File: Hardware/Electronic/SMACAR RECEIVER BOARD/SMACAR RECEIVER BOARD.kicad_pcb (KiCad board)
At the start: 2 copper layers, 9 parts, among them J1 M04POLAR, J2 USB_C_Receptacle_USB2.0_14P, U1 ESP32-S3-DevKitC

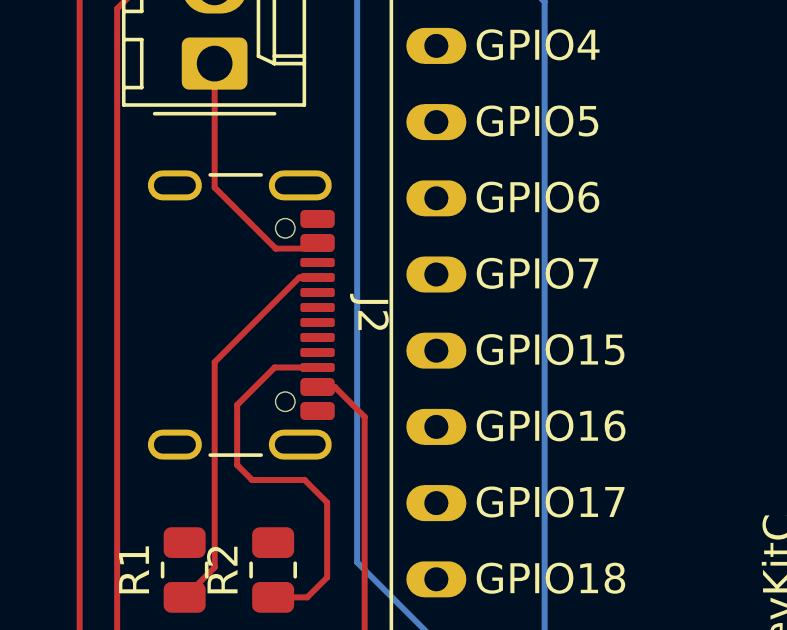
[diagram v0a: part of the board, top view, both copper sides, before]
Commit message: arreglos en las conexiones de usb c
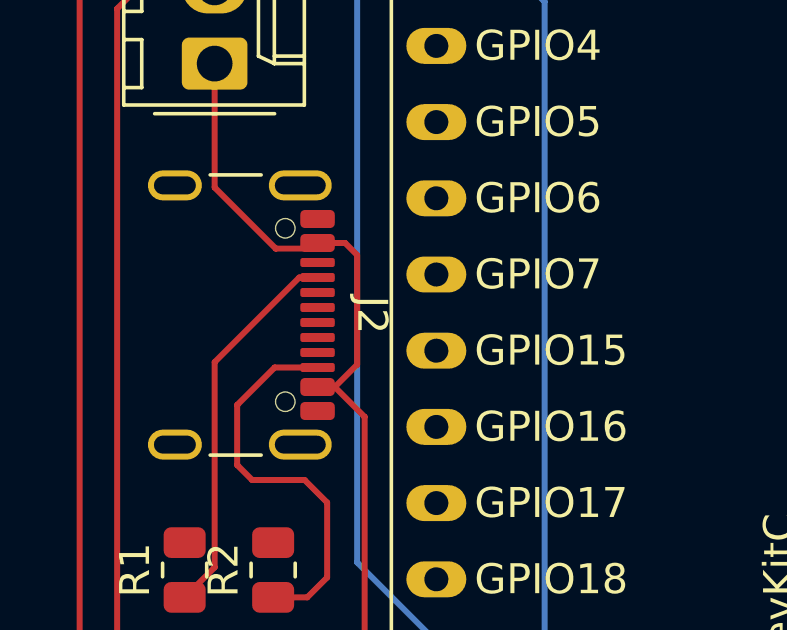
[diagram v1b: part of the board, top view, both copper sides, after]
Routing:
- net 5V: track 42.3 -> 48.5 mm
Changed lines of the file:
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@@
+	)
+	(segment
+		(start 132.35 66.1)
+		(end 131.43 66.1)
+		(width 0.2)
+		(layer "F.Cu")
+		(net 1)
 	)
 	(segment
 		(start 130.036 66.286)
 		(end 131.244 66.286)
+		(width 0.2)
+		(layer "F.Cu")
+		(net 1)
+	)
+	(segment
+		(start 132.75 66.5)
+		(end 132.35 66.1)
 		(width 0.2)
 		(layer "F.Cu")
@@
 	)
 	(segment
+		(start 132.004999 70.9)
+		(end 132.75 70.154999)
+		(width 0.2)
+		(layer "F.Cu")
+		(net 1)
+	)
+	(segment
 		(start 128 60.12)
 		(end 128 64.25)
 		(width 0.2)
 		(layer "F.Cu")
+		(net 1)
+	)
+	(segment
+		(start 132.75 70.154999)
+		(end 132.75 66.5)
+		(width 0.2)
+		(layer "F.Cu")

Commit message: TVS
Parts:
- added U2: TVS0500DRV, Package_SON:WSON-6-1EP_2x2mm_P0.65mm_EP1x1.6mm, F.Cu at (127.1, 89.3)
- added U3: TVS0500DRV, Package_SON:WSON-6-1EP_2x2mm_P0.65mm_EP1x1.6mm, F.Cu at (127.4, 102.8)
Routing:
- net Net-(R3-Pad2): track 108.6 -> 194.5 mm
- net 5V: track 48.5 -> 68.1 mm, vias 0 -> 1
- net GND: track 0.00 -> 1.30 mm

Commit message: V1.0 Revision
Revision for V1.0 of the project. Includes production files for JLCPCB. Some footprints and schematic symbols were changed.
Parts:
- removed R1, R2: 470R_0805_350mW, Resistor_SMD:R_0805_2012Metric
- removed U2, U3: TVS0500DRV, Package_SON:WSON-6-1EP_2x2mm_P0.65mm_EP1x1.6mm
- added D1: SMF33A, Diode_SMD:D_SMF, F.Cu at (131.5, 92.0)
- added D2: SMF33A, Diode_SMD:D_SMF, F.Cu at (135.0, 53.0)
- added R1_5.1k1: 470R_0805_350mW, Resistor_SMD:R_0805_2012Metric_Pad1.20x1.40mm_HandSolder, F.Cu at (129.0, 97.0)
- added R2_5.1k1: 470R_0805_350mW, Resistor_SMD:R_0805_2012Metric_Pad1.20x1.40mm_HandSolder, F.Cu at (132.0, 114.0)
- J2: value USB_C_Receptacle_USB2.0_14P -> 2137160001; footprint Connector_USB:USB_C_Receptacle_GCT_USB4105-xx-A_16P_TopMnt_Horizontal -> XUNPU TYPEC-306DDW-ARP16:MOLEX_2137160001
- moved J2 37.3 mm to (124.3, 105.6)
- moved J1 26.2 mm to (127.0, 86.3)
- moved R4 8.64 mm to (134.0, 87.0), turned to 180 degrees
- moved R3 5.00 mm to (134.0, 79.0), turned to 180 degrees
- moved U1 3.37 mm to (138.7, 51.2)
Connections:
- J2 pad A8: (no net) -> unconnected-(J2-SBU1-PadA8)
- J2 pad B8: (no net) -> unconnected-(J2-SBU2-PadB8)
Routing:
- net Net-(D2-A1): track 194.5 -> 43.4 mm, vias 1 -> 0
- net SDA: track 92.7 -> 15.6 mm
- net 5V: track 68.1 -> 41.3 mm, vias 1 -> 0
- net SCL: track 41.7 -> 17.8 mm, vias 1 -> 0
- net Net-(J2-CC2): track 13.3 -> 17.3 mm
- net GND: track 1.30 -> 0.00 mm
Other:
- board outline added: 41.5 x 70 mm

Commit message: update
PCB Y CODIGO PROTOTIPO
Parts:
- removed D1, D2: SMF33A, Diode_SMD:D_SMF
- removed R1_5.1k1, R2_5.1k1: 470R_0805_350mW, Resistor_SMD:R_0805_2012Metric_Pad1.20x1.40mm_HandSolder
- added REF**: MountingHole_2.2mm_M2_DIN965_Pad, MountingHole:MountingHole_2.2mm_M2_DIN965_Pad, F.Cu at (126.5, 52.5)
- J2: value 2137160001 -> Conn_01x02; footprint XUNPU TYPEC-306DDW-ARP16:MOLEX_2137160001 -> Connector_Molex:Molex_KK-254_AE-6410-02A_1x02_P2.54mm_Vertical
- moved J2 9.11 mm to (128.0, 97.3), turned to 90 degrees
- moved REF** 4.01 mm to (162.0, 117.0)
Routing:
- net 5V: track 41.3 -> 22.5 mm
- net Net-(J2-CC2): track 17.3 -> 0.00 mm
- net Net-(J2-CC1): track 13.1 -> 0.00 mm

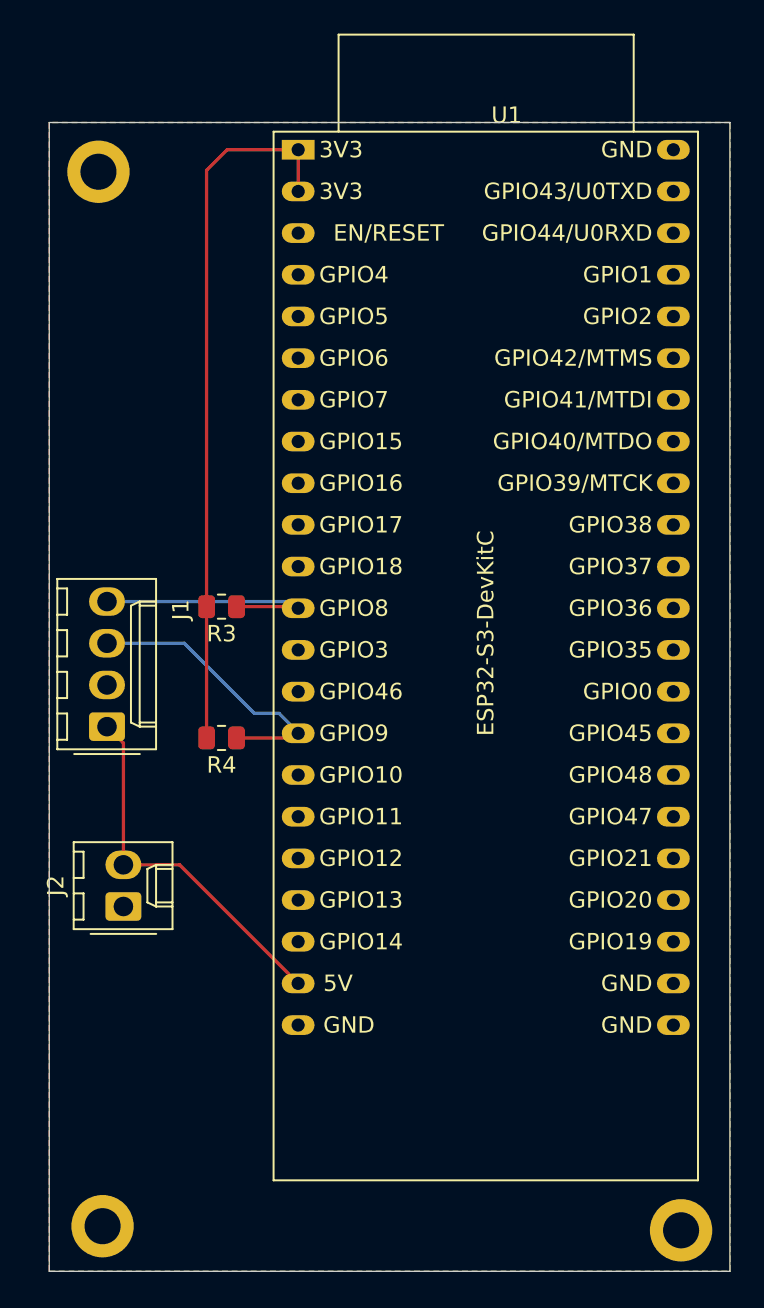
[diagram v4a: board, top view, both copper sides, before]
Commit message: PCB RECEPTOR MODIFICADA
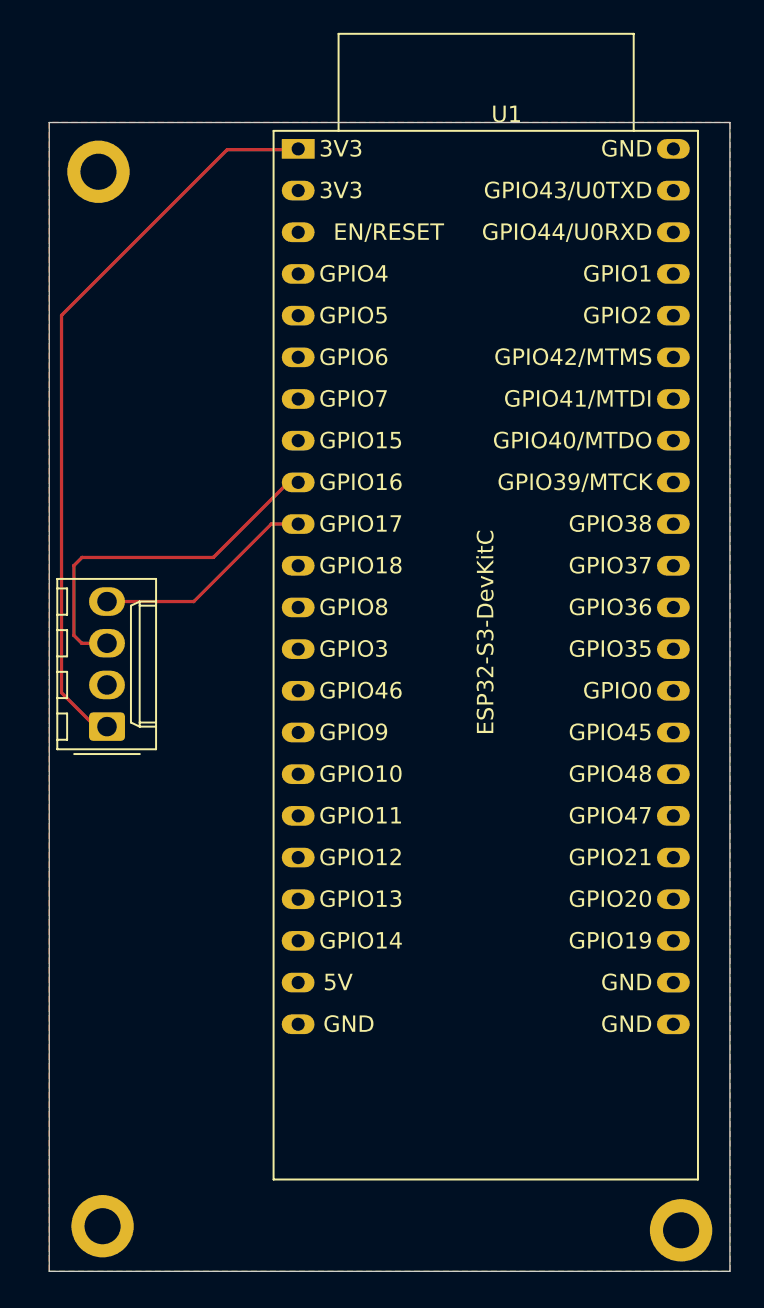
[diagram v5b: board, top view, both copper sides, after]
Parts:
- removed J2: Conn_01x02, Connector_Molex:Molex_KK-254_AE-6410-02A_1x02_P2.54mm_Vertical
- removed R3, R4: 470R_0805_350mW, Resistor_SMD:R_0805_2012Metric
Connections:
- J1 pad 1: 5V -> 3.3V
- J1 pad 3: SCL -> RX
- J1 pad 4: SDA -> TX
- U1 pad 1: Net-(D2-A1) -> 3.3V
- U1 pad 10: unconnected-(U1-GPIO17/ADC2_CH6-Pad10) -> TX
- U1 pad 12: SDA -> unconnected-(U1-GPIO8/ADC1_CH7-Pad12)
- U1 pad 15: SCL -> unconnected-(U1-GPIO9/ADC1_CH8-Pad15)
- U1 pad 2: Net-(D2-A1) -> 3.3V
- U1 pad 21: 5V -> unconnected-(U1-5V-Pad21)
- U1 pad 9: unconnected-(U1-GPIO16/ADC2_CH5/32K_N-Pad9) -> RX
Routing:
- net 3.3V: track 0.00 -> 45.2 mm
- net Net-(D2-A1): track 43.4 -> 0.00 mm
- net 5V: track 22.5 -> 0.00 mm
- net RX: track 0.00 -> 22.2 mm
- net SCL: track 17.8 -> 0.00 mm
- net SDA: track 15.6 -> 0.00 mm
- net TX: track 0.00 -> 13.6 mm
- net unconnected-(U1-GPIO8/ADC1_CH7-Pad12): track 0.00 -> 0.72 mm
- removed copper zone on B.Cu, net GND

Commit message: receptor
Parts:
- moved J1 4.13 mm to (126.2, 82.2), turned to 0 degrees
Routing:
- net 3.3V: track 45.2 -> 33.8 mm
- net RX: track 22.2 -> 13.9 mm
- net TX: track 13.6 -> 10.3 mm
- net unconnected-(U1-GPIO8/ADC1_CH7-Pad12): track 0.72 -> 0.00 mm

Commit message: PCBS
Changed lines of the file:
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@@
+		)
+		(fill no)
+		(layer "Edge.Cuts")
+	)
+	(gr_rect
+		(start 123.5 49.5)
+		(end 164.975 119.5)
+		(stroke
+			(width 0.05)
+			(type default)
 		)
 		(fill no)
@@
 		(hatch edge 0.5)
 		(connect_pads
-			(clearance 0.5)
+			(clearance 0.6)
 		)
-		(min_thickness 0.25)
+		(min_thickness 0.025)
 		(filled_areas_thickness no)
 		(fill yes
-			(thermal_gap 0.5)
-			(thermal_bridge_width 0.5)
+			(thermal_gap 0.6)
+			(thermal_bridge_width 0.6)
+			(island_removal_mode 1)
+			(island_area_min 10)
 		)
 		(polygon
 			(pts
-				(xy 123.25 49.25) (xy 165 49.5) (xy 164.5 119.25) (xy 122.5 119)
+				(xy 123.25 49.25) (xy 165 49.5) (xy 165 119.75) (xy 123.5 119.5)
 			)
 		)
